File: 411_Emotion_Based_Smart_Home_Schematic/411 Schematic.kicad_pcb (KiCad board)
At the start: 2 copper layers, 110 x 46 mm, 14 parts, among them Q1 NSS1C301ET4G, Q2 NSS1C301ET4G, Q3 NSS1C301ET4G, U4 HC-SR04

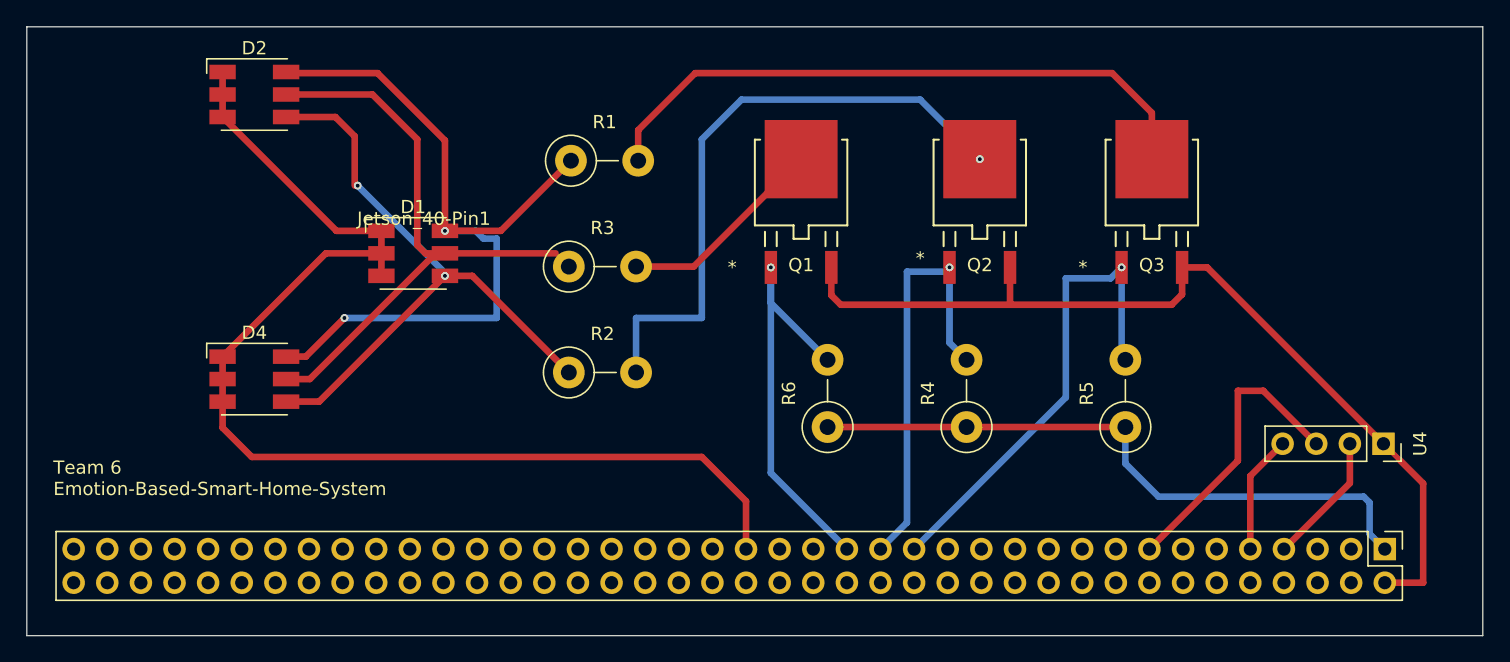
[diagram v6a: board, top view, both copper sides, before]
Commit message: Added TP and cleaned up all the traces.
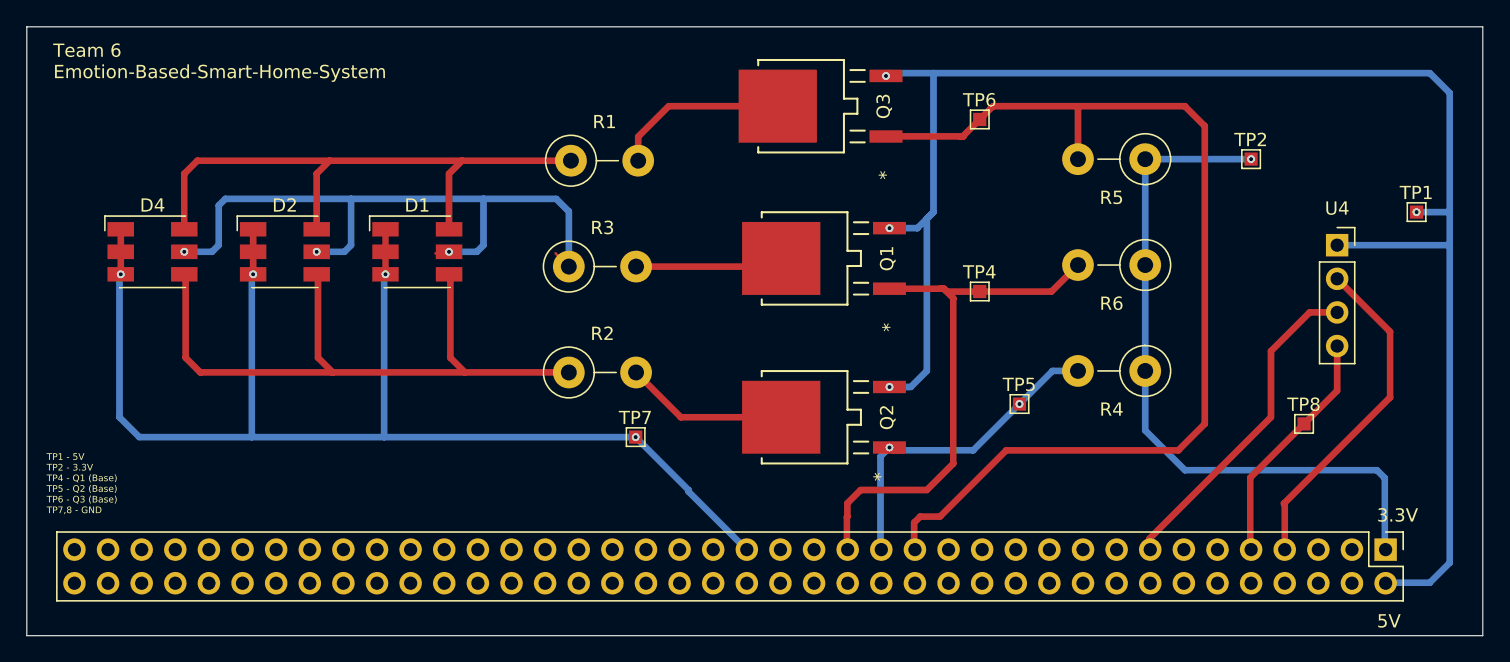
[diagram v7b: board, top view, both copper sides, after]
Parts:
- removed Jetson_40-Pin1: ~, Connector_PinHeader_2.54mm:PinHeader_2x40_P2.54mm_Vertical
- added 40_Pin_Header1: ~, Connector_PinHeader_2.54mm:PinHeader_2x40_P2.54mm_Vertical, F.Cu at (148.2, 93.5)
- added TP1: 5V, TestPoint:TestPoint_Pad_1.0x1.0mm, F.Cu at (150.5, 68.0)
- added TP2: 3.3V, TestPoint:TestPoint_Pad_1.0x1.0mm, F.Cu at (138.0, 64.0)
- added TP4: Q1, TestPoint:TestPoint_Pad_1.0x1.0mm, F.Cu at (117.5, 74.0)
- added TP5: Q2, TestPoint:TestPoint_Pad_1.0x1.0mm, F.Cu at (120.5, 82.5)
- added TP6: Q3, TestPoint:TestPoint_Pad_1.0x1.0mm, F.Cu at (117.5, 61.0)
- added TP7: GND, TestPoint:TestPoint_Pad_1.0x1.0mm, F.Cu at (91.5, 85.0)
- added TP8: GND, TestPoint:TestPoint_Pad_1.0x1.0mm, F.Cu at (142.0, 84.0)
- moved Q3 27.1 mm to (104.0, 60.0), turned to 90 degrees
- moved R6 26.9 mm to (130.0, 72.0), turned to 180 degrees
- moved Q2 22.1 mm to (104.3, 83.5), turned to 90 degrees
- moved R5 20.3 mm to (130.0, 64.0), turned to 180 degrees
- moved U4 15.4 mm to (144.5, 70.5), turned to 0 degrees
- moved R4 14.2 mm to (130.0, 80.0), turned to 180 degrees
- moved D4 12.3 mm to (55.0, 71.0)
- moved D2 12.1 mm to (65.0, 71.0)
- moved Q1 5.74 mm to (104.3, 71.5), turned to 90 degrees
- moved D1 0.33 mm to (75.0, 71.0)
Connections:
- net /5V renamed 5V
- U4 pad 2: /Ultrasonic Trigger -> /Trigger
- U4 pad 3: Net-(Jetson_40-Pin1-GPIO12) -> /Echo
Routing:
- net 5V: track 69.5 -> 125.2 mm, vias 0 -> 4
- net Net-(40_Pin_Header1-GPIO01): track 36.9 -> 79.5 mm, vias 1 -> 0
- net Net-(Q3-E): track 47.6 -> 13.3 mm
- net Net-(Q2-E): track 46.7 -> 12.4 mm, vias 1 -> 0
- net /Trigger: track 0.00 -> 25.5 mm
- net /Echo: track 0.00 -> 25.0 mm
- net Net-(Jetson_40-Pin1-GPIO12): track 22.3 -> 0.00 mm
- net Q3: track 59.9 -> 45.0 mm, vias 2 -> 0
- net /Ultrasonic Trigger: track 10.0 -> 0.00 mm
- net Net-(U4-GND): track 8.97 -> 18.1 mm
- net Net-(40_Pin_Header1-GPIO13): track 32.4 -> 41.4 mm, vias 1 -> 0
- net GND: track 88.9 -> 97.3 mm, vias 0 -> 4
- net Net-(40_Pin_Header1-GPIO11): track 32.6 -> 25.1 mm, vias 1 -> 2
- net Net-(Q1-E): track 15.8 -> 11.2 mm
- net Net-(40_Pin_Header1-3.3V): track 48.9 -> 53.5 mm, vias 0 -> 1
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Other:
- board text added: "3.3V"
- board text added: "5V"
- board text added: "TP1 - 5V TP2 - 3.3V TP4 - Q1 (Base) TP5 - Q2 (Base) TP6 - Q3 (Base) TP7,8 - GND"

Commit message: Updated schematic and layout.
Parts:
- added REF**: MountingHole_3.5mm_Pad_TopBottom, MountingHole:MountingHole_3.5mm_Pad_TopBottom, F.Cu at (158.0, 96.0)
- added REF**: MountingHole_3.5mm_Pad_TopBottom, MountingHole:MountingHole_3.5mm_Pad_TopBottom, F.Cu at (158.0, 56.0)
- added REF**: MountingHole_3.5mm_Pad_TopBottom, MountingHole:MountingHole_3.5mm_Pad_TopBottom, F.Cu at (44.0, 96.0)
- added REF**: MountingHole_3.5mm_Pad_TopBottom, MountingHole:MountingHole_3.5mm_Pad_TopBottom, F.Cu at (44.0, 56.0)
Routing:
- net 5V: track 125.2 -> 121.1 mm
- net GND: track 97.3 -> 95.2 mm
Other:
- board size 110 x 46 mm -> 123 x 48 mm
- board text added: "GND"
- board text added: "Q1 (Base)"
- board text added: "Q2 (Base)"
- board text added: "Q3 (Base)"
- board text added: "Team 6 Emotion-Based-Smart-Home-System Rev. 4 11/20/2024"
- board text removed: "TP1 - 5V TP2 - 3.3V TP4 - Q1 (Base) TP5 - Q2 (Base) TP6 - Q3 (Base) TP7,8 - GND"
- board text removed: "Team 6 Emotion-Based-Smart-Home-System"
